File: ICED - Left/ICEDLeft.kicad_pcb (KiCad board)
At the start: 2 copper layers, 175.4 x 145 mm, 164 parts, among them P1 FLASH_HDR, P2 USBC, P3 CONN_17, P4 USB3_AFEMALE, Q1 TC1264, U1 MK20DX256VLH7, U2 IS31FL3731C, X1 CRYSTAL

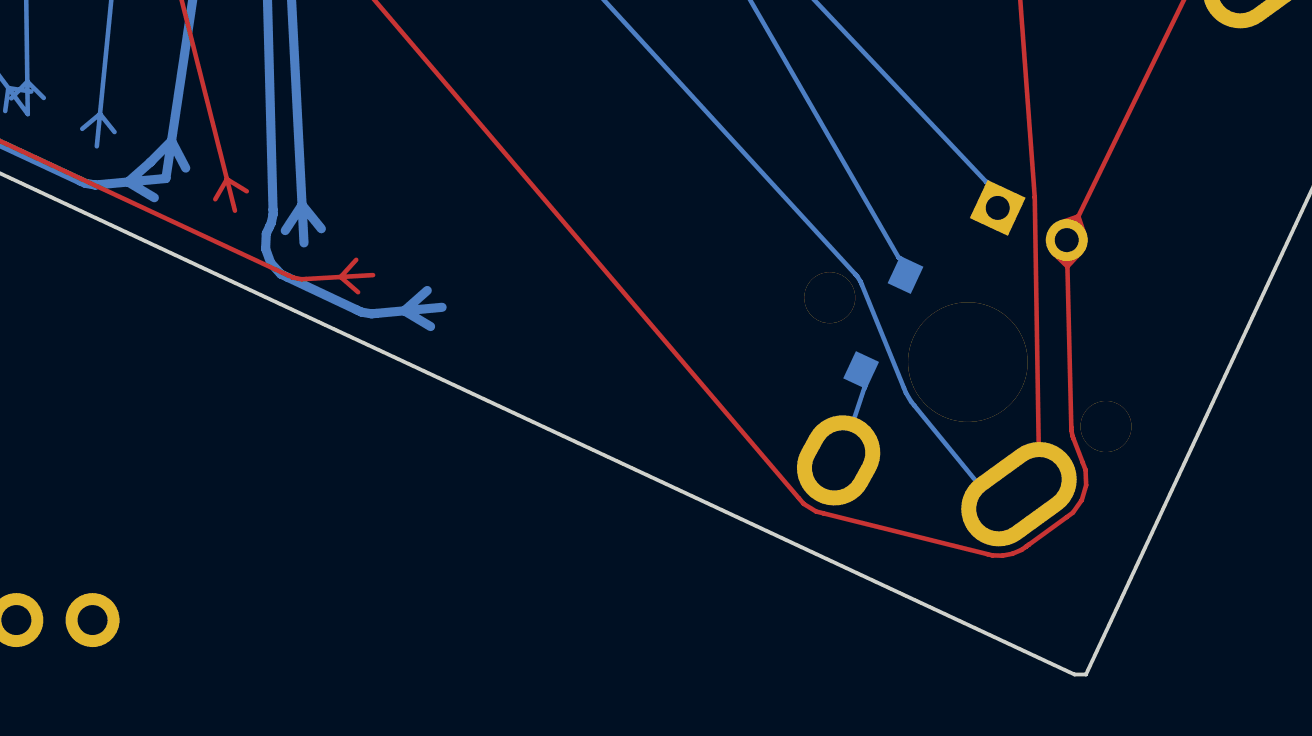
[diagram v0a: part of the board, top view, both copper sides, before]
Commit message: moved S31
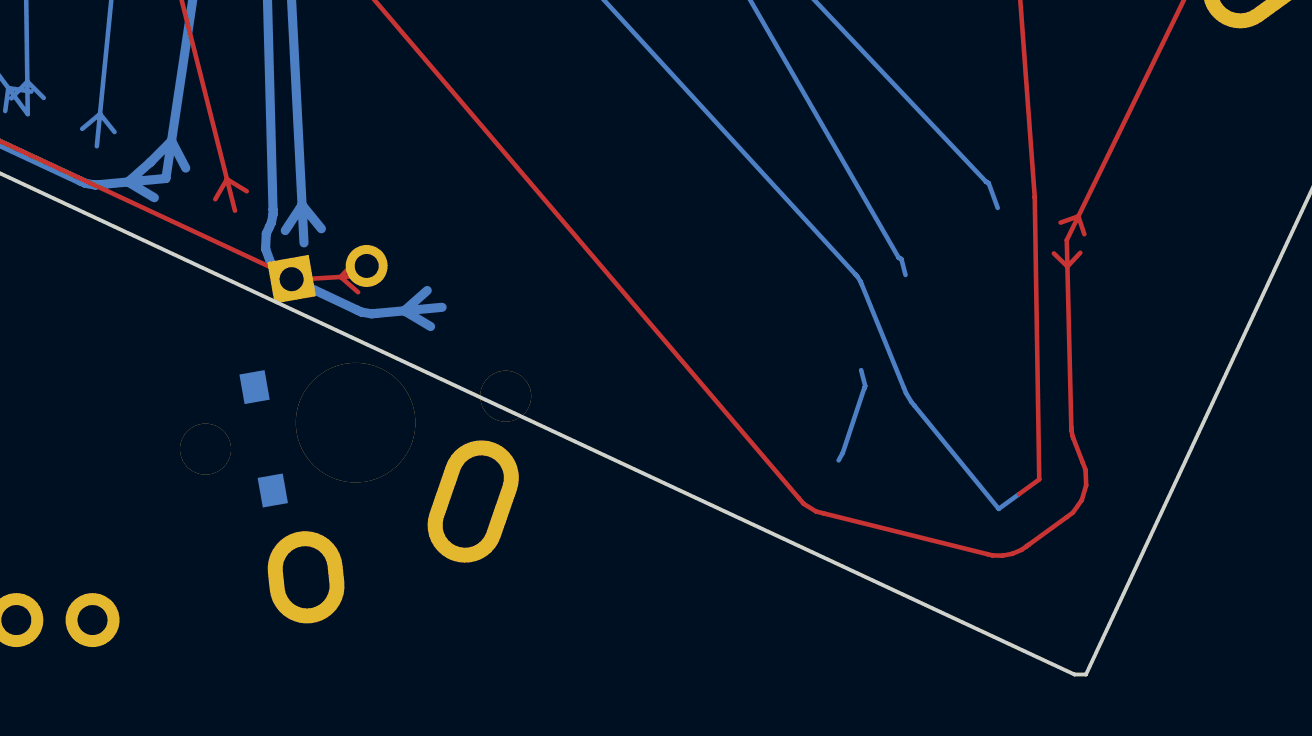
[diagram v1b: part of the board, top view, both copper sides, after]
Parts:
- moved D69 23.5 mm to (145.2, 157.4), turned to 370 degrees
- moved D31 21.0 mm to (143.0, 163.0), turned to 190 degrees
- moved S31 20.5 mm to (146.1, 162.4), turned to 190 degrees
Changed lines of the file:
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@@
   )
   (module prettylib:INSW_LEDS_REG (layer Front)
-    (at 168.643 155.798 335)
-    (attr smd)
-    (fp_text reference D69 (at 0 -1.5 335) (layer B.SilkS)
-      (effects (font (size 1 1) (thickness 0.2)) (justify mirror))
-    )
-    (fp_text value LED (at 0 2.413 335) (layer F.SilkS) hide
-      (effects (font (thickness 0.3048)))
-    )
-    (pad 2 thru_hole oval (at 1.27 0 335) (size 1.4 1.4) (drill 0.8) (layers *.Cu *.Mask F.SilkS)
+    (at 145.20637 157.41722 370)
+    (attr smd)
+    (fp_text reference D69 (at 0 -1.5 370) (layer B.SilkS)
+      (effects (font (size 1 1) (thickness 0.2)) (justify mirror))
+    )
+    (fp_text value LED (at 0 2.413 370) (layer F.SilkS) hide
+      (effects (font (thickness 0.3048)))
+    )
+    (pad 2 thru_hole oval (at 1.27 0 370) (size 1.4 1.4) (drill 0.8) (layers *.Cu *.Mask F.SilkS)
       (net 2 /ledmatrix/CA1))
-    (pad 1 thru_hole rect (at -1.27 0 335) (size 1.4 1.4) (drill 0.8) (layers *.Cu *.Mask F.SilkS)
+    (pad 1 thru_hole rect (at -1.27 0 370) (size 1.4 1.4) (drill 0.8) (layers *.Cu *.Mask F.SilkS)
       (net 9 /ledmatrix/CA8))
   )
@@
   )
   (module prettylib:SOT123-DIODE (layer Back)
-    (at 163.678 159.085 155)
-    (descr DIODE)
-    (tags DIODE)
-    (attr smd)
-    (fp_text reference D31 (at 0 3.81 425) (layer B.SilkS)
-      (effects (font (size 1.016 1.016) (thickness 0.2032)) (justify mirror))
-    )
-    (fp_text value DIODE (at 2.031999 0 425) (layer B.SilkS) hide
-      (effects (font (thickness 0.3048)) (justify mirror))
-    )
-    (fp_line (start -0.8509 0.70104) (end 0.8509 0.70104) (layer B.SilkS) (width 0.22098))
-    (fp_line (start -0.8509 1.45034) (end -0.59944 1.45034) (layer B.SilkS) (width 0.22098))
-    (fp_line (start 0.8509 1.45034) (end 0.59944 1.45034) (layer B.SilkS) (width 0.22098))
-    (fp_line (start 0.8509 -1.45034) (end 0.59944 -1.45034) (layer B.SilkS) (width 0.22098))
-    (fp_line (start -0.8509 -1.45034) (end -0.59944 -1.45034) (layer B.SilkS) (width 0.22098))
-    (fp_line (start -0.8509 -1.45034) (end -0.8509 1.45034) (layer B.SilkS) (width 0.22098))
-    (fp_line (start 0.8509 -1.45034) (end 0.8509 1.45034) (layer B.SilkS) (width 0.22098))
-    (pad 2 smd rect (at 0 1.7526 245) (size 1.00076 0.8509) (layers Back B.Paste B.Mask)
+    (at 143.02472 162.96027 190)
+    (descr DIODE)
+    (tags DIODE)
+    (attr smd)
+    (fp_text reference D31 (at 0 3.81 460) (layer B.SilkS)
+      (effects (font (size 1.016 1.016) (thickness 0.2032)) (justify mirror))
+    )
+    (fp_text value DIODE (at 2.031999 0 460) (layer B.SilkS) hide
+      (effects (font (thickness 0.3048)) (justify mirror))
+    )
+    (fp_line (start -0.8509 0.70104) (end 0.8509 0.70104) (layer B.SilkS) (width 0.22098))
+    (fp_line (start -0.8509 1.45034) (end -0.59944 1.45034) (layer B.SilkS) (width 0.22098))
+    (fp_line (start 0.8509 1.45034) (end 0.59944 1.45034) (layer B.SilkS) (width 0.22098))
+    (fp_line (start 0.8509 -1.45034) (end 0.59944 -1.45034) (layer B.SilkS) (width 0.22098))
+    (fp_line (start -0.8509 -1.45034) (end -0.59944 -1.45034) (layer B.SilkS) (width 0.22098))
+    (fp_line (start -0.8509 -1.45034) (end -0.8509 1.45034) (layer B.SilkS) (width 0.22098))
+    (fp_line (start 0.8509 -1.45034) (end 0.8509 1.45034) (layer B.SilkS) (width 0.22098))
+    (pad 2 smd rect (at 0 1.7526 280) (size 1.00076 0.8509) (layers Back B.Paste B.Mask)
       (net 101 /Row5))
-    (pad 1 smd rect (at 0 -1.74752 245) (size 1.00076 0.8509) (layers Back B.Paste B.Mask)
+    (pad 1 smd rect (at 0 -1.74752 280) (size 1.00076 0.8509) (layers Back B.Paste B.Mask)
       (net 79 "Net-(D31-Pad1)"))
   )
@@
   )
   (module prettylib:MXALPS (layer Front)
-    (at 166.497 160.401 155)
-    (descr MXALPS)
-    (tags MXALPS)
-    (fp_text reference S31 (at 0 3.048 155) (layer B.SilkS)
-      (effects (font (thickness 0.3048)) (justify mirror))
-    )
-    (fp_text value SW (at -3.5 9 155) (layer B.SilkS) hide
-      (effects (font (thickness 0.3048)) (justify mirror))
-    )
-    (fp_line (start -7.75 6.4) (end -7.75 -6.4) (layer Dwgs.User) (width 0.3))
-    (fp_line (start -7.75 6.4) (end 7.75 6.4) (layer Dwgs.User) (width 0.3))
-    (fp_line (start 7.75 6.4) (end 7.75 -6.4) (layer Dwgs.User) (width 0.3))
-    (fp_line (start 7.75 -6.4) (end -7.75 -6.4) (layer Dwgs.User) (width 0.3))
-    (fp_line (start -7.62 -7.62) (end 7.62 -7.62) (layer Dwgs.User) (width 0.3))
-    (fp_line (start 7.62 -7.62) (end 7.62 7.62) (layer Dwgs.User) (width 0.3))
-    (fp_line (start 7.62 7.62) (end -7.62 7.62) (layer Dwgs.User) (width 0.3))
-    (fp_line (start -7.62 7.62) (end -7.62 -7.62) (layer Dwgs.User) (width 0.3))
-    (pad "" np_thru_hole circle (at 0 0 155) (size 3.98781 3.98781) (drill 3.9878) (layers *.Cu *.Mask F.SilkS)
-      (clearance 0.1524))
-    (pad "" np_thru_hole circle (at -5.08 0 155) (size 1.70181 1.70181) (drill 1.7018) (layers *.Cu *.Mask F.SilkS)
-      (clearance 0.1524))
-    (pad "" np_thru_hole circle (at 5.08 0 155) (size 1.70181 1.70181) (drill 1.7018) (layers *.Cu *.Mask F.SilkS)
-      (clearance 0.1524))
-    (pad 1 thru_hole oval (at -3.405 -3.27 125.95) (size 2.5 4.17) (drill oval 1.5 3.17) (layers *.Cu *.Mask F.SilkS)
+    (at 146.08851 162.42005 190)
+    (descr MXALPS)
+    (tags MXALPS)
+    (fp_text reference S31 (at 0 3.048 190) (layer B.SilkS)
+      (effects (font (thickness 0.3048)) (justify mirror))
+    )
+    (fp_text value SW (at -3.5 9 190) (layer B.SilkS) hide
+      (effects (font (thickness 0.3048)) (justify mirror))
+    )
+    (fp_line (start -7.75 6.4) (end -7.75 -6.4) (layer Dwgs.User) (width 0.3))
+    (fp_line (start -7.75 6.4) (end 7.75 6.4) (layer Dwgs.User) (width 0.3))
+    (fp_line (start 7.75 6.4) (end 7.75 -6.4) (layer Dwgs.User) (width 0.3))
+    (fp_line (start 7.75 -6.4) (end -7.75 -6.4) (layer Dwgs.User) (width 0.3))
+    (fp_line (start -7.62 -7.62) (end 7.62 -7.62) (layer Dwgs.User) (width 0.3))
+    (fp_line (start 7.62 -7.62) (end 7.62 7.62) (layer Dwgs.User) (width 0.3))
+    (fp_line (start 7.62 7.62) (end -7.62 7.62) (layer Dwgs.User) (width 0.3))
+    (fp_line (start -7.62 7.62) (end -7.62 -7.62) (layer Dwgs.User) (width 0.3))
+    (pad "" np_thru_hole circle (at 0 0 190) (size 3.98781 3.98781) (drill 3.9878) (layers *.Cu *.Mask F.SilkS)
+      (clearance 0.1524))
+    (pad "" np_thru_hole circle (at -5.08 0 190) (size 1.70181 1.70181) (drill 1.7018) (layers *.Cu *.Mask F.SilkS)
+      (clearance 0.1524))
+    (pad "" np_thru_hole circle (at 5.08 0 190) (size 1.70181 1.70181) (drill 1.7018) (layers *.Cu *.Mask F.SilkS)
+      (clearance 0.1524))
+    (pad 1 thru_hole oval (at -3.405 -3.27 160.95) (size 2.5 4.17) (drill oval 1.5 3.17) (layers *.Cu *.Mask F.SilkS)
       (net 121 /Col2))
-    (pad 2 thru_hole oval (at 2.52 -4.79 151.1) (size 2.5 3.08) (drill oval 1.5 2.08) (layers *.Cu *.Mask F.SilkS)
+    (pad 2 thru_hole oval (at 2.52 -4.79 186.1) (size 2.5 3.08) (drill oval 1.5 2.08) (layers *.Cu *.Mask F.SilkS)
       (net 79 "Net-(D31-Pad1)"))
   )

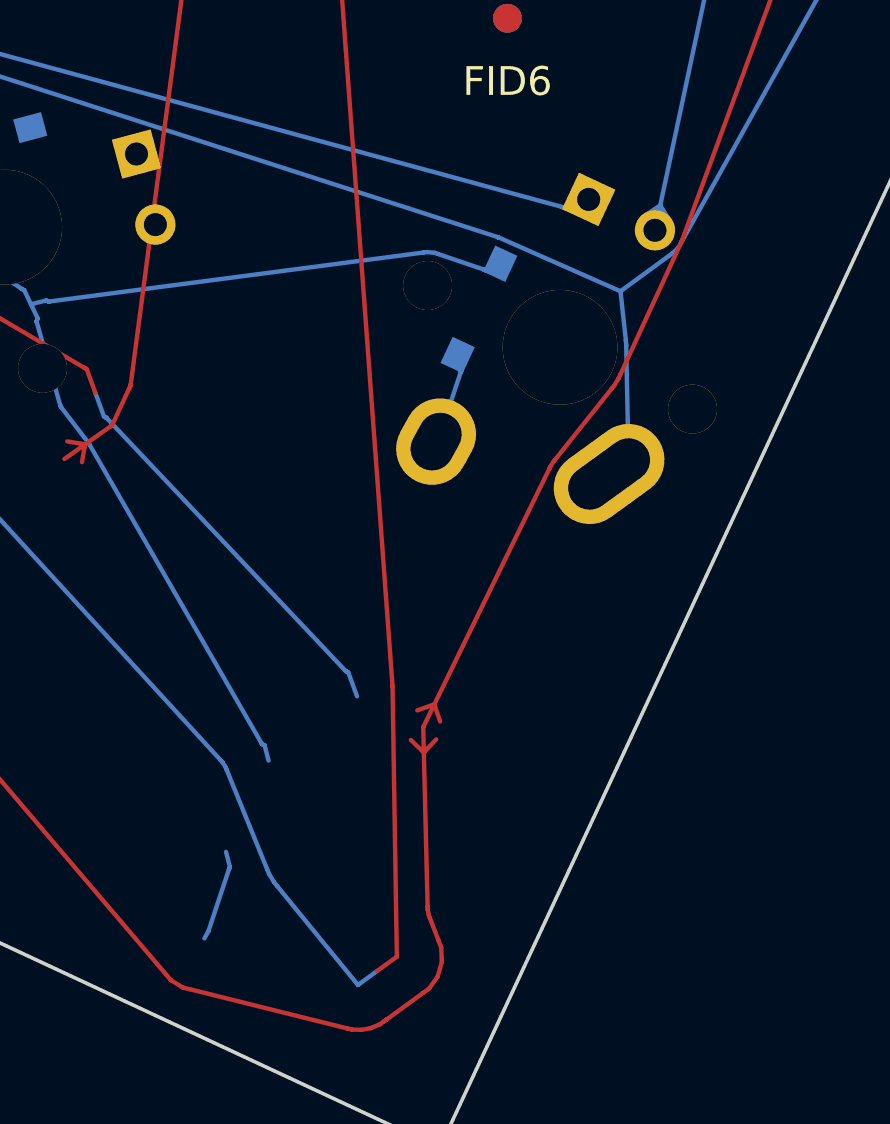
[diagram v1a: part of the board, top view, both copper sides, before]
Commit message: moved S30
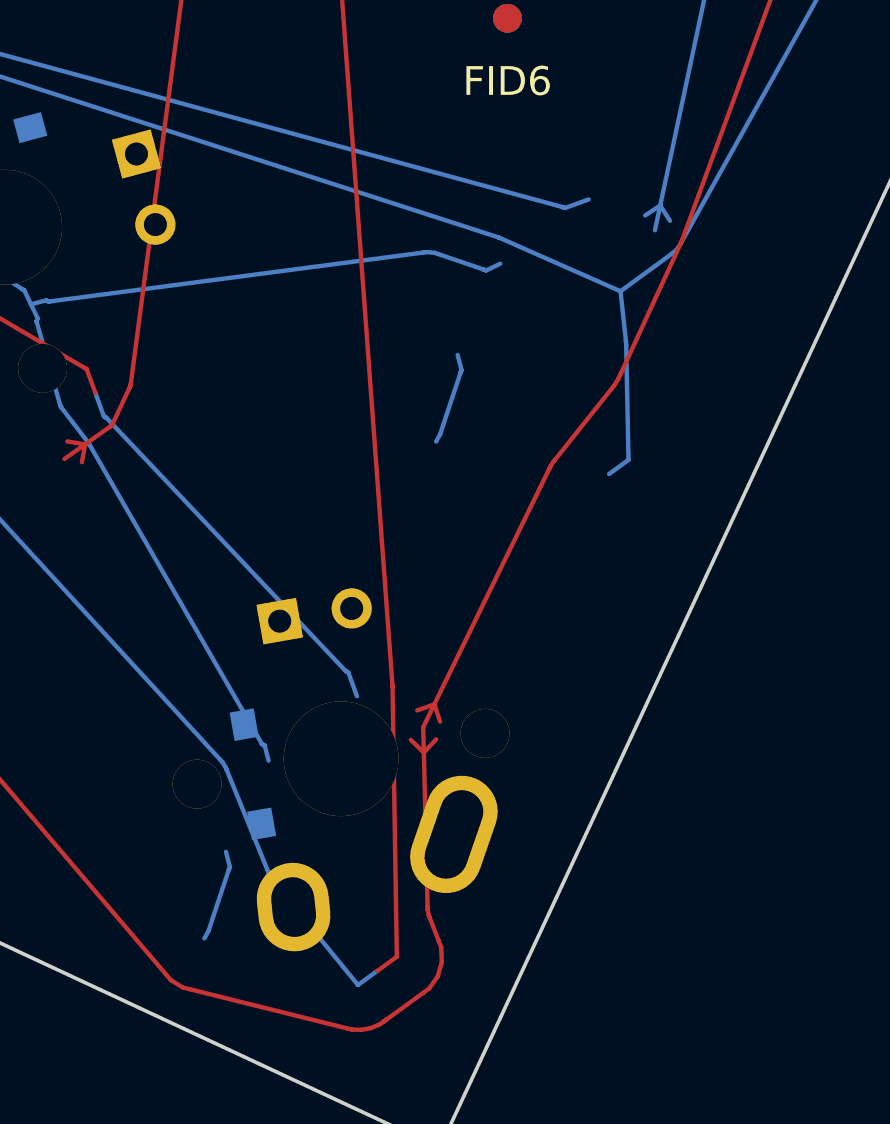
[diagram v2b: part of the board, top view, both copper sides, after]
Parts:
- moved D30 18.0 mm to (163.9, 158.0), turned to 190 degrees
- moved D68 17.5 mm to (166.1, 152.4), turned to 370 degrees
- moved S30 16.2 mm to (166.9, 157.4), turned to 190 degrees
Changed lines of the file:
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@@
   )
   (module prettylib:INSW_LEDS_REG (layer Front)
-    (at 176.695 138.531 335)
-    (attr smd)
-    (fp_text reference D68 (at 0 -1.5 335) (layer B.SilkS)
-      (effects (font (size 1 1) (thickness 0.2)) (justify mirror))
-    )
-    (fp_text value LED (at 0 2.413 335) (layer F.SilkS) hide
-      (effects (font (thickness 0.3048)))
-    )
-    (pad 2 thru_hole oval (at 1.27 0 335) (size 1.4 1.4) (drill 0.8) (layers *.Cu *.Mask F.SilkS)
+    (at 166.05707 152.42972 370)
+    (attr smd)
+    (fp_text reference D68 (at 0 -1.5 370) (layer B.SilkS)
+      (effects (font (size 1 1) (thickness 0.2)) (justify mirror))
+    )
+    (fp_text value LED (at 0 2.413 370) (layer F.SilkS) hide
+      (effects (font (thickness 0.3048)))
+    )
+    (pad 2 thru_hole oval (at 1.27 0 370) (size 1.4 1.4) (drill 0.8) (layers *.Cu *.Mask F.SilkS)
       (net 6 /ledmatrix/CA5))
-    (pad 1 thru_hole rect (at -1.27 0 335) (size 1.4 1.4) (drill 0.8) (layers *.Cu *.Mask F.SilkS)
+    (pad 1 thru_hole rect (at -1.27 0 370) (size 1.4 1.4) (drill 0.8) (layers *.Cu *.Mask F.SilkS)
       (net 8 /ledmatrix/CA7))
   )
@@
   )
   (module prettylib:SOT123-DIODE (layer Back)
-    (at 171.729 141.818 155)
-    (descr DIODE)
-    (tags DIODE)
-    (attr smd)
-    (fp_text reference D30 (at 0 3.81 425) (layer B.SilkS)
-      (effects (font (size 1.016 1.016) (thickness 0.2032)) (justify mirror))
-    )
-    (fp_text value DIODE (at 2.031999 0 425) (layer B.SilkS) hide
-      (effects (font (thickness 0.3048)) (justify mirror))
-    )
-    (fp_line (start -0.8509 0.70104) (end 0.8509 0.70104) (layer B.SilkS) (width 0.22098))
-    (fp_line (start -0.8509 1.45034) (end -0.59944 1.45034) (layer B.SilkS) (width 0.22098))
-    (fp_line (start 0.8509 1.45034) (end 0.59944 1.45034) (layer B.SilkS) (width 0.22098))
-    (fp_line (start 0.8509 -1.45034) (end 0.59944 -1.45034) (layer B.SilkS) (width 0.22098))
-    (fp_line (start -0.8509 -1.45034) (end -0.59944 -1.45034) (layer B.SilkS) (width 0.22098))
-    (fp_line (start -0.8509 -1.45034) (end -0.8509 1.45034) (layer B.SilkS) (width 0.22098))
-    (fp_line (start 0.8509 -1.45034) (end 0.8509 1.45034) (layer B.SilkS) (width 0.22098))
-    (pad 2 smd rect (at 0 1.7526 245) (size 1.00076 0.8509) (layers Back B.Paste B.Mask)
+    (at 163.87453 157.97293 190)
+    (descr DIODE)
+    (tags DIODE)
+    (attr smd)
+    (fp_text reference D30 (at 0 3.81 460) (layer B.SilkS)
+      (effects (font (size 1.016 1.016) (thickness 0.2032)) (justify mirror))
+    )
+    (fp_text value DIODE (at 2.031999 0 460) (layer B.SilkS) hide
+      (effects (font (thickness 0.3048)) (justify mirror))
+    )
+    (fp_line (start -0.8509 0.70104) (end 0.8509 0.70104) (layer B.SilkS) (width 0.22098))
+    (fp_line (start -0.8509 1.45034) (end -0.59944 1.45034) (layer B.SilkS) (width 0.22098))
+    (fp_line (start 0.8509 1.45034) (end 0.59944 1.45034) (layer B.SilkS) (width 0.22098))
+    (fp_line (start 0.8509 -1.45034) (end 0.59944 -1.45034) (layer B.SilkS) (width 0.22098))
+    (fp_line (start -0.8509 -1.45034) (end -0.59944 -1.45034) (layer B.SilkS) (width 0.22098))
+    (fp_line (start -0.8509 -1.45034) (end -0.8509 1.45034) (layer B.SilkS) (width 0.22098))
+    (fp_line (start 0.8509 -1.45034) (end 0.8509 1.45034) (layer B.SilkS) (width 0.22098))
+    (pad 2 smd rect (at 0 1.7526 280) (size 1.00076 0.8509) (layers Back B.Paste B.Mask)
       (net 101 /Row5))
-    (pad 1 smd rect (at 0 -1.74752 245) (size 1.00076 0.8509) (layers Back B.Paste B.Mask)
+    (pad 1 smd rect (at 0 -1.74752 280) (size 1.00076 0.8509) (layers Back B.Paste B.Mask)
       (net 78 "Net-(D30-Pad1)"))
   )
@@
   )
   (module prettylib:MXALPS (layer Front)
-    (at 174.549 143.134 155)
-    (descr MXALPS)
-    (tags MXALPS)
-    (fp_text reference S30 (at 0 3.048 155) (layer B.SilkS)
-      (effects (font (thickness 0.3048)) (justify mirror))
-    )
-    (fp_text value SW (at -3.5 9 155) (layer B.SilkS) hide
-      (effects (font (thickness 0.3048)) (justify mirror))
-    )
-    (fp_line (start -7.75 6.4) (end -7.75 -6.4) (layer Dwgs.User) (width 0.3))
-    (fp_line (start -7.75 6.4) (end 7.75 6.4) (layer Dwgs.User) (width 0.3))
-    (fp_line (start 7.75 6.4) (end 7.75 -6.4) (layer Dwgs.User) (width 0.3))
-    (fp_line (start 7.75 -6.4) (end -7.75 -6.4) (layer Dwgs.User) (width 0.3))
-    (fp_line (start -7.62 -7.62) (end 7.62 -7.62) (layer Dwgs.User) (width 0.3))
-    (fp_line (start 7.62 -7.62) (end 7.62 7.62) (layer Dwgs.User) (width 0.3))
-    (fp_line (start 7.62 7.62) (end -7.62 7.62) (layer Dwgs.User) (width 0.3))
-    (fp_line (start -7.62 7.62) (end -7.62 -7.62) (layer Dwgs.User) (width 0.3))
-    (pad "" np_thru_hole circle (at 0 0 155) (size 3.98781 3.98781) (drill 3.9878) (layers *.Cu *.Mask F.SilkS)
-      (clearance 0.1524))
-    (pad "" np_thru_hole circle (at -5.08 0 155) (size 1.70181 1.70181) (drill 1.7018) (layers *.Cu *.Mask F.SilkS)
-      (clearance 0.1524))
-    (pad "" np_thru_hole circle (at 5.08 0 155) (size 1.70181 1.70181) (drill 1.7018) (layers *.Cu *.Mask F.SilkS)
-      (clearance 0.1524))
-    (pad 1 thru_hole oval (at -3.405 -3.27 125.95) (size 2.5 4.17) (drill oval 1.5 3.17) (layers *.Cu *.Mask F.SilkS)
+    (at 166.9392 157.43255 190)
+    (descr MXALPS)
+    (tags MXALPS)
+    (fp_text reference S30 (at 0 3.048 190) (layer B.SilkS)
+      (effects (font (thickness 0.3048)) (justify mirror))
+    )
+    (fp_text value SW (at -3.5 9 190) (layer B.SilkS) hide
+      (effects (font (thickness 0.3048)) (justify mirror))
+    )
+    (fp_line (start -7.75 6.4) (end -7.75 -6.4) (layer Dwgs.User) (width 0.3))
+    (fp_line (start -7.75 6.4) (end 7.75 6.4) (layer Dwgs.User) (width 0.3))
+    (fp_line (start 7.75 6.4) (end 7.75 -6.4) (layer Dwgs.User) (width 0.3))
+    (fp_line (start 7.75 -6.4) (end -7.75 -6.4) (layer Dwgs.User) (width 0.3))
+    (fp_line (start -7.62 -7.62) (end 7.62 -7.62) (layer Dwgs.User) (width 0.3))
+    (fp_line (start 7.62 -7.62) (end 7.62 7.62) (layer Dwgs.User) (width 0.3))
+    (fp_line (start 7.62 7.62) (end -7.62 7.62) (layer Dwgs.User) (width 0.3))
+    (fp_line (start -7.62 7.62) (end -7.62 -7.62) (layer Dwgs.User) (width 0.3))
+    (pad "" np_thru_hole circle (at 0 0 190) (size 3.98781 3.98781) (drill 3.9878) (layers *.Cu *.Mask F.SilkS)
+      (clearance 0.1524))
+    (pad "" np_thru_hole circle (at -5.08 0 190) (size 1.70181 1.70181) (drill 1.7018) (layers *.Cu *.Mask F.SilkS)
+      (clearance 0.1524))
+    (pad "" np_thru_hole circle (at 5.08 0 190) (size 1.70181 1.70181) (drill 1.7018) (layers *.Cu *.Mask F.SilkS)
+      (clearance 0.1524))
+    (pad 1 thru_hole oval (at -3.405 -3.27 160.95) (size 2.5 4.17) (drill oval 1.5 3.17) (layers *.Cu *.Mask F.SilkS)
       (net 120 /Col1))
-    (pad 2 thru_hole oval (at 2.52 -4.79 151.1) (size 2.5 3.08) (drill oval 1.5 2.08) (layers *.Cu *.Mask F.SilkS)
+    (pad 2 thru_hole oval (at 2.52 -4.79 186.1) (size 2.5 3.08) (drill oval 1.5 2.08) (layers *.Cu *.Mask F.SilkS)
       (net 78 "Net-(D30-Pad1)"))
   )
